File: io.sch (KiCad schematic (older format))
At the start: 5 parts, among them J1 USB_2, P3 DIN_5, P4 DIN_5, P5 CONN_5, U5 OPTO-TRANSISTOR4

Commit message: Package updates
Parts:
- removed J1: USB_2, symbol USB_2
- removed P3, P4: DIN_5, symbol DIN_5
- added P1, P3, P4, P6: CONN_5, symbol CONN_5
- added Q1: PDTA124X, SOT23-3, symbol PDTA124X
- added Q2: PDTC123Y, SOT23-3, symbol PDTC123Y
- added R12: 1.5k, symbol R
- added R13, R14: DNP, symbol R
- added R15, R16, R17, R8: 220, symbol R
- U5: value OPTO-TRANSISTOR4 -> VOL617A
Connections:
- net labels added: +3.3V, +5V, GND
- wire segments 0 -> 36
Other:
- note removed: "micro-USB has five pins..."
- moved on the sheet: U5

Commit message: Changes.
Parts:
- removed P5: CONN_5, symbol CONN_5
- added P5: CONN_4, symbol CONN_4
- R8: value 220 -> 20k
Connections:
- net +3.3V: now also P5.1 (P1)
- net GND: now also P5.4 (P4)
- net PGM_RX: now also P5.2 (P2)
- net PGM_TX: now also P5.3 (P3)
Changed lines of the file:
@@
-EESchema Schematic File Version 2  date Sat 14 Apr 2012 04:28:33 PM CEST
+EESchema Schematic File Version 2  date Sat 14 Apr 2012 07:12:50 PM CEST
 LIBS:power
 LIBS:device
@@
 LIBS:dogs102-6
 LIBS:pdt-transistor
+LIBS:tact
 LIBS:knobboard-cache
 EELAYER 25  0
@@
 $EndDescr
 $Comp
-L +3.3V #PWR?
+L CONN_4 P5
+U 1 1 4F898BCF
+P 5850 5950
+F 0 "P5" V 5800 5950 50  0000 C CNN
+F 1 "CONN_4" V 5900 5950 50  0000 C CNN
+	1    5850 5950
+	1    0    0    -1
+$EndComp
+Wire Wire Line
+	5400 6350 5400 6100
+Wire Wire Line
+	5400 6100 5500 6100
+Wire Wire Line
+	5200 5900 5500 5900
+Wire Wire Line
+	4000 3450 4000 3300
+Wire Wire Line
+	4000 3300 4200 3300
+Wire Wire Line
+	4200 3000 3800 3000
+Wire Wire Line
+	4800 4750 4450 4750
+Connection ~ 6550 3000
+Wire Wire Line
+	6550 3000 6550 3750
+Wire Wire Line
+	6550 3750 7450 3750
+Wire Wire Line
+	6800 4500 6300 4500
+Wire Wire Line
+	6300 4500 6300 4250
+Wire Wire Line
+	5900 3000 5450 3000
+Wire Wire Line
+	7350 4200 7350 4050
+Wire Wire Line
+	7350 4050 7450 4050
+Wire Wire Line
+	7450 3950 6800 3950
+Wire Wire Line
+	6800 3950 6800 4400
+Connection ~ 6800 1600
+Wire Wire Line
+	6800 1450 6800 1600
+Wire Wire Line
+	6950 1700 5950 1700
+Wire Wire Line
+	6150 2100 6150 1900
+Wire Wire Line
+	6150 1900 5950 1900
+Wire Wire Line
+	5950 1500 6150 1500
+Wire Wire Line
+	6150 1500 6150 1350
+Wire Wire Line
+	6950 1600 5950 1600
+Wire Wire Line
+	6600 1450 6600 1700
+Connection ~ 6600 1700
+Wire Wire Line
+	5950 1800 6600 1800
+Wire Wire Line
+	6800 4700 6550 4700
+Wire Wire Line
+	6550 4700 6550 4900
+Wire Wire Line
+	7450 3850 6700 3850
+Wire Wire Line
+	6700 3850 6700 4500
+Connection ~ 6700 4500
+Wire Wire Line
+	6400 3000 6750 3000
+Wire Wire Line
+	5450 3300 5700 3300
+Wire Wire Line
+	5700 3300 5700 2900
+Wire Wire Line
+	5700 2900 6750 2900
+Wire Wire Line
+	6800 4400 6100 4400
+Wire Wire Line
+	6650 2900 6650 3650
+Wire Wire Line
+	6650 3650 7450 3650
+Connection ~ 6650 2900
+Wire Wire Line
+	5350 4400 5600 4400
+Wire Wire Line
+	3750 4400 3900 4400
+Wire Wire Line
+	4000 2900 4000 3000
+Connection ~ 4000 3000
+Wire Wire Line
+	5400 5750 5400 5800
+Wire Wire Line
+	5400 5800 5500 5800
+Wire Wire Line
+	5500 6000 5200 6000
+$Comp
+L GND #PWR06
+U 1 1 4F898B55
+P 5400 6350
+F 0 "#PWR06" H 5400 6350 30  0001 C CNN
+F 1 "GND" H 5400 6280 30  0001 C CNN
+	1    5400 6350
+	1    0    0    -1
+$EndComp
+$Comp
+L +3.3V #PWR07
+U 1 1 4F898B22
+P 5400 5750
+F 0 "#PWR07" H 5400 5710 30  0001 C CNN
+F 1 "+3.3V" H 5400 5860 30  0000 C CNN
+	1    5400 5750
+	1    0    0    -1
+$EndComp
+$Comp
+L +3.3V #PWR08
 U 1 1 4F8985F8
 P 4000 2400
-F 0 "#PWR?" H 4000 2360 30  0001 C CNN
+F 0 "#PWR08" H 4000 2360 30  0001 C CNN
 F 1 "+3.3V" H 4000 2510 30  0000 C CNN
 	1    4000 2400
 	1    0    0    -1
 $EndComp
-Wire Wire Line
-	4000 3450 4000 3300
-Wire Wire Line
-	4000 3300 4200 3300
-Wire Wire Line
-	4200 3000 3800 3000
-Wire Wire Line
-	4800 4750 4450 4750
-Connection ~ 6550 3000
-Wire Wire Line
-	6550 3000 6550 3750
-Wire Wire Line
-	6550 3750 7450 3750
-Wire Wire Line
-	6800 4500 6300 4500
-Wire Wire Line
-	6300 4500 6300 4250
-Wire Wire Line
-	5900 3000 5450 3000
-Wire Wire Line
-	7350 4200 7350 4050
-Wire Wire Line
-	7350 4050 7450 4050
-Wire Wire Line
-	7450 3950 6800 3950
-Wire Wire Line
-	6800 3950 6800 4400
-Connection ~ 6800 1600
-Wire Wire Line
-	6800 1450 6800 1600
-Wire Wire Line
-	6950 1700 5950 1700
-Wire Wire Line
-	6150 2100 6150 1900
-Wire Wire Line
-	6150 1900 5950 1900
-Wire Wire Line
-	5950 1500 6150 1500
-Wire Wire Line
-	6150 1500 6150 1350
-Wire Wire Line
-	6950 1600 5950 1600
-Wire Wire Line
-	6600 1450 6600 1700
-Connection ~ 6600 1700
-Wire Wire Line
-	5950 1800 6600 1800
-Wire Wire Line
-	6800 4700 6550 4700
-Wire Wire Line
-	6550 4700 6550 4900
-Wire Wire Line
-	7450 3850 6700 3850
-Wire Wire Line
-	6700 3850 6700 4500
-Connection ~ 6700 4500
-Wire Wire Line
-	6400 3000 6750 3000
-Wire Wire Line
-	5450 3300 5700 3300
-Wire Wire Line
-	5700 3300 5700 2900
-Wire Wire Line
-	5700 2900 6750 2900
-Wire Wire Line
-	6800 4400 6100 4400
-Wire Wire Line
-	6650 2900 6650 3650
-Wire Wire Line
-	6650 3650 7450 3650
-Connection ~ 6650 2900
-Wire Wire Line
-	5350 4400 5600 4400
-Wire Wire Line
-	3750 4400 3900 4400
-Wire Wire Line
-	4000 2900 4000 3000
-Connection ~ 4000 3000
-$Comp
-L GND #PWR06
+$Comp
+L GND #PWR09
 U 1 1 4F8984E9
 P 4000 3450
-F 0 "#PWR06" H 4000 3450 30  0001 C CNN
+F 0 "#PWR09" H 4000 3450 30  0001 C CNN
 F 1 "GND" H 4000 3380 30  0001 C CNN
 	1    4000 3450
@@
 P 4000 2650
 F 0 "R8" V 4080 2650 50  0000 C CNN
-F 1 "220" V 4000 2650 50  0000 C CNN
+F 1 "20k" V 4000 2650 50  0000 C CNN
 	1    4000 2650
 	-1   0    0    1
 $EndComp
 $Comp
-L +3.3V #PWR07
+L +3.3V #PWR010
 U 1 1 4F898360
 P 4450 3950
-F 0 "#PWR07" H 4450 3910 30  0001 C CNN
+F 0 "#PWR010" H 4450 3910 30  0001 C CNN
 F 1 "+3.3V" H 4450 4060 30  0000 C CNN
 	1    4450 3950
@@
 $EndComp
 $Comp
-L GND #PWR08
+L GND #PWR011
 U 1 1 4F897803
 P 5350 5200
-F 0 "#PWR08" H 5350 5200 30  0001 C CNN
+F 0 "#PWR011" H 5350 5200 30  0001 C CNN
 F 1 "GND" H 5350 5130 30  0001 C CNN
 	1    5350 5200
@@
 $EndComp
 $Comp
-L GND #PWR09
+L GND #PWR012
 U 1 1 4F896AAD
 P 7350 4200
-F 0 "#PWR09" H 7350 4200 30  0001 C CNN
+F 0 "#PWR012" H 7350 4200 30  0001 C CNN
 F 1 "GND" H 7350 4130 30  0001 C CNN
 	1    7350 4200
@@
 $EndComp
 $Comp
-L GND #PWR010
+L GND #PWR013
 U 1 1 4F896A83
 P 6550 4900
-F 0 "#PWR010" H 6550 4900 30  0001 C CNN
+F 0 "#PWR013" H 6550 4900 30  0001 C CNN
 F 1 "GND" H 6550 4830 30  0001 C CNN
 	1    6550 4900
@@
 $EndComp
 $Comp
-L +5V #PWR011
+L +5V #PWR014
 U 1 1 4F8968A2
 P 6300 3750
-F 0 "#PWR011" H 6300 3840 20  0001 C CNN
+F 0 "#PWR014" H 6300 3840 20  0001 C CNN
 F 1 "+5V" H 6300 3840 30  0000 C CNN
 	1    6300 3750
@@
 $EndComp
 $Comp
-L GND #PWR012
+L GND #PWR015
 U 1 1 4F894AD1
 P 6600 2300
-F 0 "#PWR012" H 6600 2300 30  0001 C CNN
+F 0 "#PWR015" H 6600 2300 30  0001 C CNN
 F 1 "GND" H 6600 2230 30  0001 C CNN
 	1    6600 2300
@@
 $EndComp
 $Comp
-L +3.3V #PWR013
+L +3.3V #PWR016
 U 1 1 4F894691
 P 6800 950
-F 0 "#PWR013" H 6800 910 30  0001 C CNN
+F 0 "#PWR016" H 6800 910 30  0001 C CNN
 F 1 "+3.3V" H 6800 1060 30  0000 C CNN
 	1    6800 950
@@
 $EndComp
 $Comp
-L +3.3V #PWR014
+L +3.3V #PWR017
 U 1 1 4F89446F
 P 6600 950
-F 0 "#PWR014" H 6600 910 30  0001 C CNN
+F 0 "#PWR017" H 6600 910 30  0001 C CNN
 F 1 "+3.3V" H 6600 1060 30  0000 C CNN
 	1    6600 950
@@
 $EndComp
 $Comp
-L GND #PWR015
+L GND #PWR018
 U 1 1 4F894376
 P 6150 2100
-F 0 "#PWR015" H 6150 2100 30  0001 C CNN
+F 0 "#PWR018" H 6150 2100 30  0001 C CNN
 F 1 "GND" H 6150 2030 30  0001 C CNN
 	1    6150 2100
@@
 $EndComp
 $Comp
-L +5V #PWR016
+L +5V #PWR019
 U 1 1 4F894373
 P 6150 1350
-F 0 "#PWR016" H 6150 1440 20  0001 C CNN
+F 0 "#PWR019" H 6150 1440 20  0001 C CNN
 F 1 "+5V" H 6150 1440 30  0000 C CNN
 	1    6150 1350
@@
 	-1   0    0    -1
 $EndComp
-$Comp
-L CONN_5 P5
-U 1 1 4F8179DB
-P 5900 6000
-F 0 "P5" V 5850 6000 50  0000 C CNN
-F 1 "CONN_5" V 5950 6000 50  0000 C CNN
-	1    5900 6000
-	1    0    0    -1
-$EndComp
-Text HLabel 5200 6050 0    60   Input ~ 0
+Text HLabel 5200 6000 0    60   Input ~ 0
 PGM_TX
 Text HLabel 5200 5900 0    60   Output ~ 0

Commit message: Floorplanning
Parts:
- added P7: CONN_2, symbol CONN_2
- added R10: 0, symbol R
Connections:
- net +5V: now also P7.2 (PM), R10.1; no longer P1.1
- net MIDIIN+: now reaches R16.2, U5.1 (A)
- net MIDIIN-: now reaches P3.5, P6.5, U5.2 (K)
- net USB_ID: now reaches P1.4, R13.1
- net MIDIOUT-: now reaches P4.5, P6.2, R15.1
- net MIDIOUT+: now reaches P4.4, P6.3, R17.1
- new net USB_5V: P1.1, P7.1 (P1), R10.2
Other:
- note added: "Programming with bootloader (USART1)"
- note added: "USB"
- moved on the sheet: P1, Q1, Q2, R15, R16, R17
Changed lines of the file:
@@
-EESchema Schematic File Version 2  date Sat 14 Apr 2012 07:12:50 PM CEST
+EESchema Schematic File Version 2  date Sun 15 Apr 2012 10:50:25 AM CEST
 LIBS:power
 LIBS:device
@@
 Sheet 3 5
 Title ""
-Date "14 apr 2012"
+Date "15 apr 2012"
 Rev ""
 Comp ""
@@
 Comment4 ""
 $EndDescr
+Text Notes 6150 5950 0    60   ~ 0
+Programming with bootloader (USART1)
+Text Label 5850 4500 0    60   ~ 0
+MIDIOUT+
+Text Label 5850 4400 0    60   ~ 0
+MIDIOUT-
+Wire Wire Line
+	5550 4400 6800 4400
+Wire Wire Line
+	5250 1300 5950 1300
+Wire Wire Line
+	6150 1450 6150 1500
+Wire Wire Line
+	5500 6000 5200 6000
+Wire Wire Line
+	5500 5800 5400 5800
+Wire Wire Line
+	5400 5800 5400 5750
+Connection ~ 4000 3000
+Wire Wire Line
+	4000 2900 4000 3000
+Wire Wire Line
+	3200 4400 3350 4400
+Wire Wire Line
+	4800 4400 5050 4400
+Connection ~ 6650 2900
+Wire Wire Line
+	7450 3650 6650 3650
+Wire Wire Line
+	6650 3650 6650 2900
+Wire Wire Line
+	6750 2900 6450 2900
+Wire Wire Line
+	6450 2900 6450 3300
+Wire Wire Line
+	6450 3300 5450 3300
+Wire Wire Line
+	6350 3000 6750 3000
+Connection ~ 6700 4500
+Wire Wire Line
+	6700 4500 6700 3850
+Wire Wire Line
+	6700 3850 7450 3850
+Wire Wire Line
+	6550 4900 6550 4700
+Wire Wire Line
+	6550 4700 6800 4700
+Wire Wire Line
+	5300 1800 6600 1800
+Connection ~ 6600 1700
+Wire Wire Line
+	6600 1450 6600 1700
+Wire Wire Line
+	6950 1600 5300 1600
+Wire Wire Line
+	6150 1500 5300 1500
+Wire Wire Line
+	5300 1900 6150 1900
+Wire Wire Line
+	6150 1900 6150 2100
+Wire Wire Line
+	6950 1700 5300 1700
+Wire Wire Line
+	6800 1450 6800 1600
+Connection ~ 6800 1600
+Wire Wire Line
+	6800 4400 6800 3950
+Wire Wire Line
+	6800 3950 7450 3950
+Wire Wire Line
+	7450 4050 7350 4050
+Wire Wire Line
+	7350 4050 7350 4200
+Wire Wire Line
+	5850 3000 5450 3000
+Wire Wire Line
+	5700 4250 5700 4500
+Wire Wire Line
+	5700 4500 6800 4500
+Wire Wire Line
+	7450 3750 6550 3750
+Wire Wire Line
+	6550 3750 6550 3000
+Connection ~ 6550 3000
+Wire Wire Line
+	4250 4750 3900 4750
+Wire Wire Line
+	4200 3000 3800 3000
+Wire Wire Line
+	4200 3300 4000 3300
+Wire Wire Line
+	4000 3300 4000 3450
+Wire Wire Line
+	5200 5900 5500 5900
+Wire Wire Line
+	5500 6100 5400 6100
+Wire Wire Line
+	5400 6100 5400 6350
+Wire Wire Line
+	5250 1100 5250 950
+Wire Wire Line
+	5250 950  6150 950
+Wire Wire Line
+	5950 1300 5950 1500
+Connection ~ 5950 1500
+Text Label 5500 3300 0    60   ~ 0
+MIDIIN-
+Text Label 5500 3000 0    60   ~ 0
+MIDIIN+
+Text Label 5350 1800 0    60   ~ 0
+USB_ID
+Text Label 5350 1500 0    60   ~ 0
+USB_5V
+Text Notes 4450 1550 1    60   ~ 0
+USB
+$Comp
+L CONN_2 P7
+U 1 1 4F8A6AE1
+P 4900 1200
+F 0 "P7" V 4850 1200 40  0000 C CNN
+F 1 "CONN_2" V 4950 1200 40  0000 C CNN
+	1    4900 1200
+	-1   0    0    1
+$EndComp
+$Comp
+L R R10
+U 1 1 4F8A6AAA
+P 6150 1200
+F 0 "R10" V 6230 1200 50  0000 C CNN
+F 1 "0" V 6150 1200 50  0000 C CNN
+	1    6150 1200
+	1    0    0    -1
+$EndComp
 $Comp
 L CONN_4 P5
@@
 	1    0    0    -1
 $EndComp
-Wire Wire Line
-	5400 6350 5400 6100
-Wire Wire Line
-	5400 6100 5500 6100
-Wire Wire Line
-	5200 5900 5500 5900
-Wire Wire Line
-	4000 3450 4000 3300
-Wire Wire Line
-	4000 3300 4200 3300
-Wire Wire Line
-	4200 3000 3800 3000
-Wire Wire Line
-	4800 4750 4450 4750
-Connection ~ 6550 3000
-Wire Wire Line
-	6550 3000 6550 3750
-Wire Wire Line
-	6550 3750 7450 3750
-Wire Wire Line
-	6800 4500 6300 4500
-Wire Wire Line
-	6300 4500 6300 4250
-Wire Wire Line
-	5900 3000 5450 3000
-Wire Wire Line
-	7350 4200 7350 4050
-Wire Wire Line
-	7350 4050 7450 4050
-Wire Wire Line
-	7450 3950 6800 3950
-Wire Wire Line
-	6800 3950 6800 4400
-Connection ~ 6800 1600
-Wire Wire Line
-	6800 1450 6800 1600
-Wire Wire Line
-	6950 1700 5950 1700
-Wire Wire Line
-	6150 2100 6150 1900
-Wire Wire Line
-	6150 1900 5950 1900
-Wire Wire Line
-	5950 1500 6150 1500
-Wire Wire Line
-	6150 1500 6150 1350
-Wire Wire Line
-	6950 1600 5950 1600
-Wire Wire Line
-	6600 1450 6600 1700
-Connection ~ 6600 1700
-Wire Wire Line
-	5950 1800 6600 1800
-Wire Wire Line
-	6800 4700 6550 4700
-Wire Wire Line
-	6550 4700 6550 4900
-Wire Wire Line
-	7450 3850 6700 3850
-Wire Wire Line
-	6700 3850 6700 4500
-Connection ~ 6700 4500
-Wire Wire Line
-	6400 3000 6750 3000
-Wire Wire Line
-	5450 3300 5700 3300
-Wire Wire Line
-	5700 3300 5700 2900
-Wire Wire Line
-	5700 2900 6750 2900
-Wire Wire Line
-	6800 4400 6100 4400
-Wire Wire Line
-	6650 2900 6650 3650
-Wire Wire Line
-	6650 3650 7450 3650
-Connection ~ 6650 2900
-Wire Wire Line
-	5350 4400 5600 4400
-Wire Wire Line
-	3750 4400 3900 4400
-Wire Wire Line
-	4000 2900 4000 3000
-Connection ~ 4000 3000
-Wire Wire Line
-	5400 5750 5400 5800
-Wire Wire Line
-	5400 5800 5500 5800
-Wire Wire Line
-	5500 6000 5200 6000
 $Comp
 L GND #PWR06
@@
 L +3.3V #PWR010
 U 1 1 4F898360
-P 4450 3950
-F 0 "#PWR010" H 4450 3910 30  0001 C CNN
-F 1 "+3.3V" H 4450 4060 30  0000 C CNN
-	1    4450 3950
+P 3900 3950
+F 0 "#PWR010" H 3900 3910 30  0001 C CNN
+F 1 "+3.3V" H 3900 4060 30  0000 C CNN
+	1    3900 3950
 	1    0    0    -1
 $EndComp
@@
 L PDTA124X Q1
 U 1 1 4F898311
-P 4350 4400
-F 0 "Q1" H 4550 4300 50  0000 C CNN
-F 1 "PDTA124X" H 4600 4550 50  0000 C CNN
-F 2 "SOT23-3" H 4540 4400 30  0001 C CNN
-	1    4350 4400
+P 3800 4400
+F 0 "Q1" H 4000 4300 50  0000 C CNN
+F 1 "PDTA124X" H 4050 4550 50  0000 C CNN
+F 2 "SOT23-3" H 3990 4400 30  0001 C CNN
+	1    3800 4400
 	1    0    0    1
 $EndComp
@@
 L PDTC123Y Q2
 U 1 1 4F898308
-P 5250 4750
-F 0 "Q2" H 5450 4650 50  0000 C CNN
-F 1 "PDTC123Y" H 5500 4900 50  0000 C CNN
-F 2 "SOT23-3" H 5440 4750 30  0001 C CNN
-	1    5250 4750
+P 4700 4750
+F 0 "Q2" H 4900 4650 50  0000 C CNN
+F 1 "PDTC123Y" H 4950 4900 50  0000 C CNN
+F 2 "SOT23-3" H 4890 4750 30  0001 C CNN
+	1    4700 4750
 	1    0    0    -1
 $EndComp
@@
 L GND #PWR011
 U 1 1 4F897803
-P 5350 5200
-F 0 "#PWR011" H 5350 5200 30  0001 C CNN
-F 1 "GND" H 5350 5130 30  0001 C CNN
-	1    5350 5200
+P 4800 5200
+F 0 "#PWR011" H 4800 5200 30  0001 C CNN
+F 1 "GND" H 4800 5130 30  0001 C CNN
+	1    4800 5200
 	1    0    0    -1
 $EndComp
@@
 L R R16
 U 1 1 4F896ACC
-P 6150 3000
-F 0 "R16" V 6230 3000 50  0000 C CNN
-F 1 "220" V 6150 3000 50  0000 C CNN
-	1    6150 3000
+P 6100 3000
+F 0 "R16" V 6180 3000 50  0000 C CNN
+F 1 "220" V 6100 3000 50  0000 C CNN
+	1    6100 3000
 	0    1    1    0
 $EndComp
@@
 L R R17
 U 1 1 4F896936
-P 6300 4000
-F 0 "R17" V 6380 4000 50  0000 C CNN
-F 1 "220" V 6300 4000 50  0000 C CNN
-	1    6300 4000
+P 5700 4000
+F 0 "R17" V 5780 4000 50  0000 C CNN
+F 1 "220" V 5700 4000 50  0000 C CNN
+	1    5700 4000
 	-1   0    0    1
 $EndComp
@@
 L R R15
 U 1 1 4F896930
-P 5850 4400
-F 0 "R15" V 5930 4400 50  0000 C CNN
-F 1 "220" V 5850 4400 50  0000 C CNN
-	1    5850 4400
+P 5300 4400
+F 0 "R15" V 5380 4400 50  0000 C CNN
+F 1 "220" V 5300 4400 50  0000 C CNN
+	1    5300 4400
 	0    1    1    0
 $EndComp
@@
 L +5V #PWR014
 U 1 1 4F8968A2
-P 6300 3750
-F 0 "#PWR014" H 6300 3840 20  0001 C CNN
-F 1 "+5V" H 6300 3840 30  0000 C CNN
-	1    6300 3750
+P 5700 3750
+F 0 "#PWR014" H 5700 3840 20  0001 C CNN
+F 1 "+5V" H 5700 3840 30  0000 C CNN
+	1    5700 3750
 	1    0    0    -1
 $EndComp
@@
 L +5V #PWR019
 U 1 1 4F894373
-P 6150 1350
-F 0 "#PWR019" H 6150 1440 20  0001 C CNN
-F 1 "+5V" H 6150 1440 30  0000 C CNN
-	1    6150 1350
+P 6150 950
+F 0 "#PWR019" H 6150 1040 20  0001 C CNN
+F 1 "+5V" H 6150 1040 30  0000 C CNN
+	1    6150 950
 	1    0    0    -1
 $EndComp
@@
 L CONN_5 P1
 U 1 1 4F894357
-P 5550 1700
-F 0 "P1" V 5500 1700 50  0000 C CNN
-F 1 "CONN_5" V 5600 1700 50  0000 C CNN
-	1    5550 1700
+P 4900 1700
+F 0 "P1" V 4850 1700 50  0000 C CNN
+F 1 "CONN_5" V 4950 1700 50  0000 C CNN
+	1    4900 1700
 	-1   0    0    -1
 $EndComp
@@
 Text HLabel 6950 1700 2    60   BiDi ~ 0
 USB_DP
-Text HLabel 3750 4400 0    60   Input ~ 0
+Text HLabel 3200 4400 0    60   Input ~ 0
 MIDI_TX
 Text HLabel 3800 3000 0    60   Output ~ 0

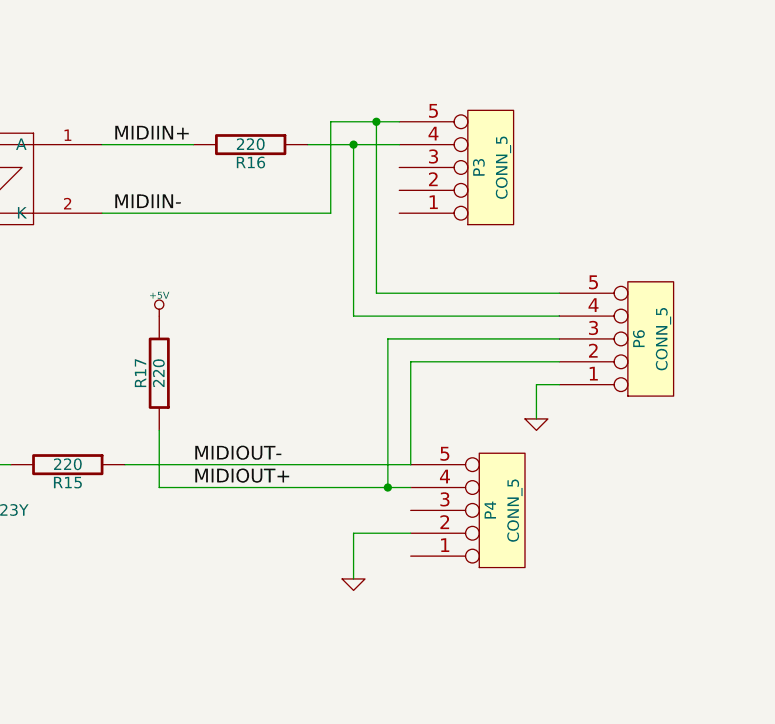
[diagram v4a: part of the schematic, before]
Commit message: Switch to shift registers. Routing.
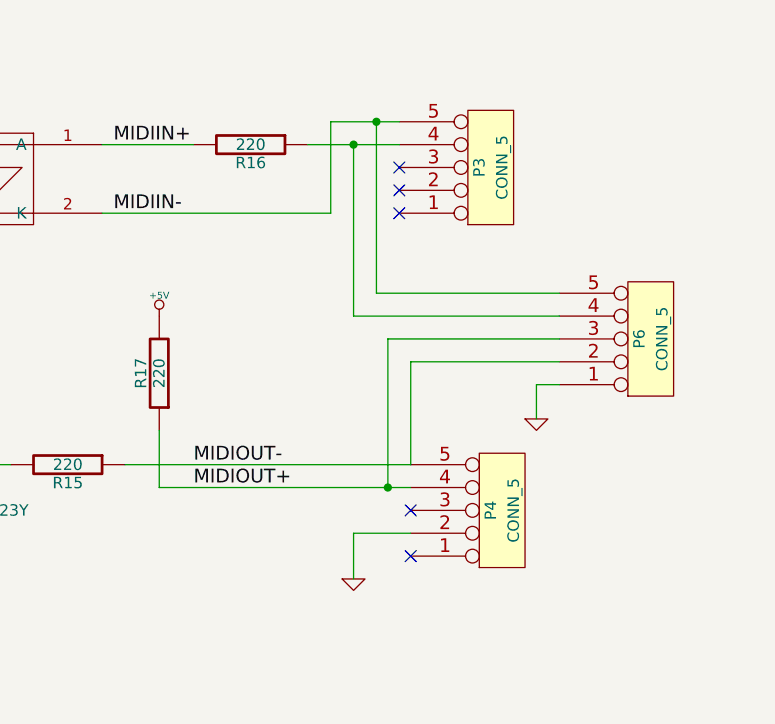
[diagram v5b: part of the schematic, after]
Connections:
- no-connect marks 0 -> 5
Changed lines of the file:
@@
-EESchema Schematic File Version 2  date Sun 15 Apr 2012 10:50:25 AM CEST
+EESchema Schematic File Version 2  date Tue 17 Apr 2012 08:42:54 PM CEST
 LIBS:power
 LIBS:device
@@
 $Descr A4 11700 8267
 encoding utf-8
-Sheet 3 5
+Sheet 4 5
 Title ""
-Date "15 apr 2012"
+Date "17 apr 2012"
 Rev ""
 Comp ""
@@
 Comment4 ""
 $EndDescr
+NoConn ~ 6800 4800
+NoConn ~ 6800 4600
+NoConn ~ 6750 3300
+NoConn ~ 6750 3200
+NoConn ~ 6750 3100
 Text Notes 6150 5950 0    60   ~ 0
 Programming with bootloader (USART1)
@@
 $EndComp
 $Comp
-L GND #PWR06
+L GND #PWR028
 U 1 1 4F898B55
 P 5400 6350
-F 0 "#PWR06" H 5400 6350 30  0001 C CNN
+F 0 "#PWR028" H 5400 6350 30  0001 C CNN
 F 1 "GND" H 5400 6280 30  0001 C CNN
 	1    5400 6350
@@
 $EndComp
 $Comp
-L +3.3V #PWR07
+L +3.3V #PWR029
 U 1 1 4F898B22
 P 5400 5750
-F 0 "#PWR07" H 5400 5710 30  0001 C CNN
+F 0 "#PWR029" H 5400 5710 30  0001 C CNN
 F 1 "+3.3V" H 5400 5860 30  0000 C CNN
 	1    5400 5750
@@
 $EndComp
 $Comp
-L +3.3V #PWR08
+L +3.3V #PWR030
 U 1 1 4F8985F8
 P 4000 2400
-F 0 "#PWR08" H 4000 2360 30  0001 C CNN
+F 0 "#PWR030" H 4000 2360 30  0001 C CNN
 F 1 "+3.3V" H 4000 2510 30  0000 C CNN
 	1    4000 2400
@@
 $EndComp
 $Comp
-L GND #PWR09
+L GND #PWR031
 U 1 1 4F8984E9
 P 4000 3450
-F 0 "#PWR09" H 4000 3450 30  0001 C CNN
+F 0 "#PWR031" H 4000 3450 30  0001 C CNN
 F 1 "GND" H 4000 3380 30  0001 C CNN
 	1    4000 3450
@@
 $EndComp
 $Comp
-L +3.3V #PWR010
+L +3.3V #PWR032
 U 1 1 4F898360
 P 3900 3950
-F 0 "#PWR010" H 3900 3910 30  0001 C CNN
+F 0 "#PWR032" H 3900 3910 30  0001 C CNN
 F 1 "+3.3V" H 3900 4060 30  0000 C CNN
 	1    3900 3950
@@
 $EndComp
 $Comp
-L GND #PWR011
+L GND #PWR033
 U 1 1 4F897803
 P 4800 5200
-F 0 "#PWR011" H 4800 5200 30  0001 C CNN
+F 0 "#PWR033" H 4800 5200 30  0001 C CNN
 F 1 "GND" H 4800 5130 30  0001 C CNN
 	1    4800 5200
@@
 $EndComp
 $Comp
-L GND #PWR012
+L GND #PWR034
 U 1 1 4F896AAD
 P 7350 4200
-F 0 "#PWR012" H 7350 4200 30  0001 C CNN
+F 0 "#PWR034" H 7350 4200 30  0001 C CNN
 F 1 "GND" H 7350 4130 30  0001 C CNN
 	1    7350 4200
@@
 $EndComp
 $Comp
-L GND #PWR013
+L GND #PWR035
 U 1 1 4F896A83
 P 6550 4900
-F 0 "#PWR013" H 6550 4900 30  0001 C CNN
+F 0 "#PWR035" H 6550 4900 30  0001 C CNN
 F 1 "GND" H 6550 4830 30  0001 C CNN
 	1    6550 4900
@@
 $EndComp
 $Comp
-L +5V #PWR014
+L +5V #PWR036
 U 1 1 4F8968A2
 P 5700 3750
-F 0 "#PWR014" H 5700 3840 20  0001 C CNN
+F 0 "#PWR036" H 5700 3840 20  0001 C CNN
 F 1 "+5V" H 5700 3840 30  0000 C CNN
 	1    5700 3750
@@
 $EndComp
 $Comp
-L GND #PWR015
+L GND #PWR037
 U 1 1 4F894AD1
 P 6600 2300
-F 0 "#PWR015" H 6600 2300 30  0001 C CNN
+F 0 "#PWR037" H 6600 2300 30  0001 C CNN
 F 1 "GND" H 6600 2230 30  0001 C CNN
 	1    6600 2300
@@
 $EndComp
 $Comp
-L +3.3V #PWR016
+L +3.3V #PWR038
 U 1 1 4F894691
 P 6800 950
-F 0 "#PWR016" H 6800 910 30  0001 C CNN
+F 0 "#PWR038" H 6800 910 30  0001 C CNN
 F 1 "+3.3V" H 6800 1060 30  0000 C CNN
 	1    6800 950
@@
 $EndComp
 $Comp
-L +3.3V #PWR017
+L +3.3V #PWR039
 U 1 1 4F89446F
 P 6600 950
-F 0 "#PWR017" H 6600 910 30  0001 C CNN
+F 0 "#PWR039" H 6600 910 30  0001 C CNN
 F 1 "+3.3V" H 6600 1060 30  0000 C CNN
 	1    6600 950
@@
 $EndComp
 $Comp
-L GND #PWR018
+L GND #PWR040
 U 1 1 4F894376
 P 6150 2100
-F 0 "#PWR018" H 6150 2100 30  0001 C CNN
+F 0 "#PWR040" H 6150 2100 30  0001 C CNN
 F 1 "GND" H 6150 2030 30  0001 C CNN
 	1    6150 2100
@@
 $EndComp
 $Comp
-L +5V #PWR019
+L +5V #PWR041
 U 1 1 4F894373
 P 6150 950
-F 0 "#PWR019" H 6150 1040 20  0001 C CNN
+F 0 "#PWR041" H 6150 1040 20  0001 C CNN
 F 1 "+5V" H 6150 1040 30  0000 C CNN
 	1    6150 950
